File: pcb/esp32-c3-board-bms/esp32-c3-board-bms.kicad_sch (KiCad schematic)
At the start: 34 parts, among them P1 HW-613, P101 CAN, P102 BMS UART, P3 CONN_1, P4 CONN_1, P5 CONN_1, P6 CONN_1, U1 ESP32-C3-Waveshare, U102 TJA1050, U2 esp32-c3-ebay, U3 LP2985-3.3, U4 PC817, U5 DCDCConverter, U7 STIS0621

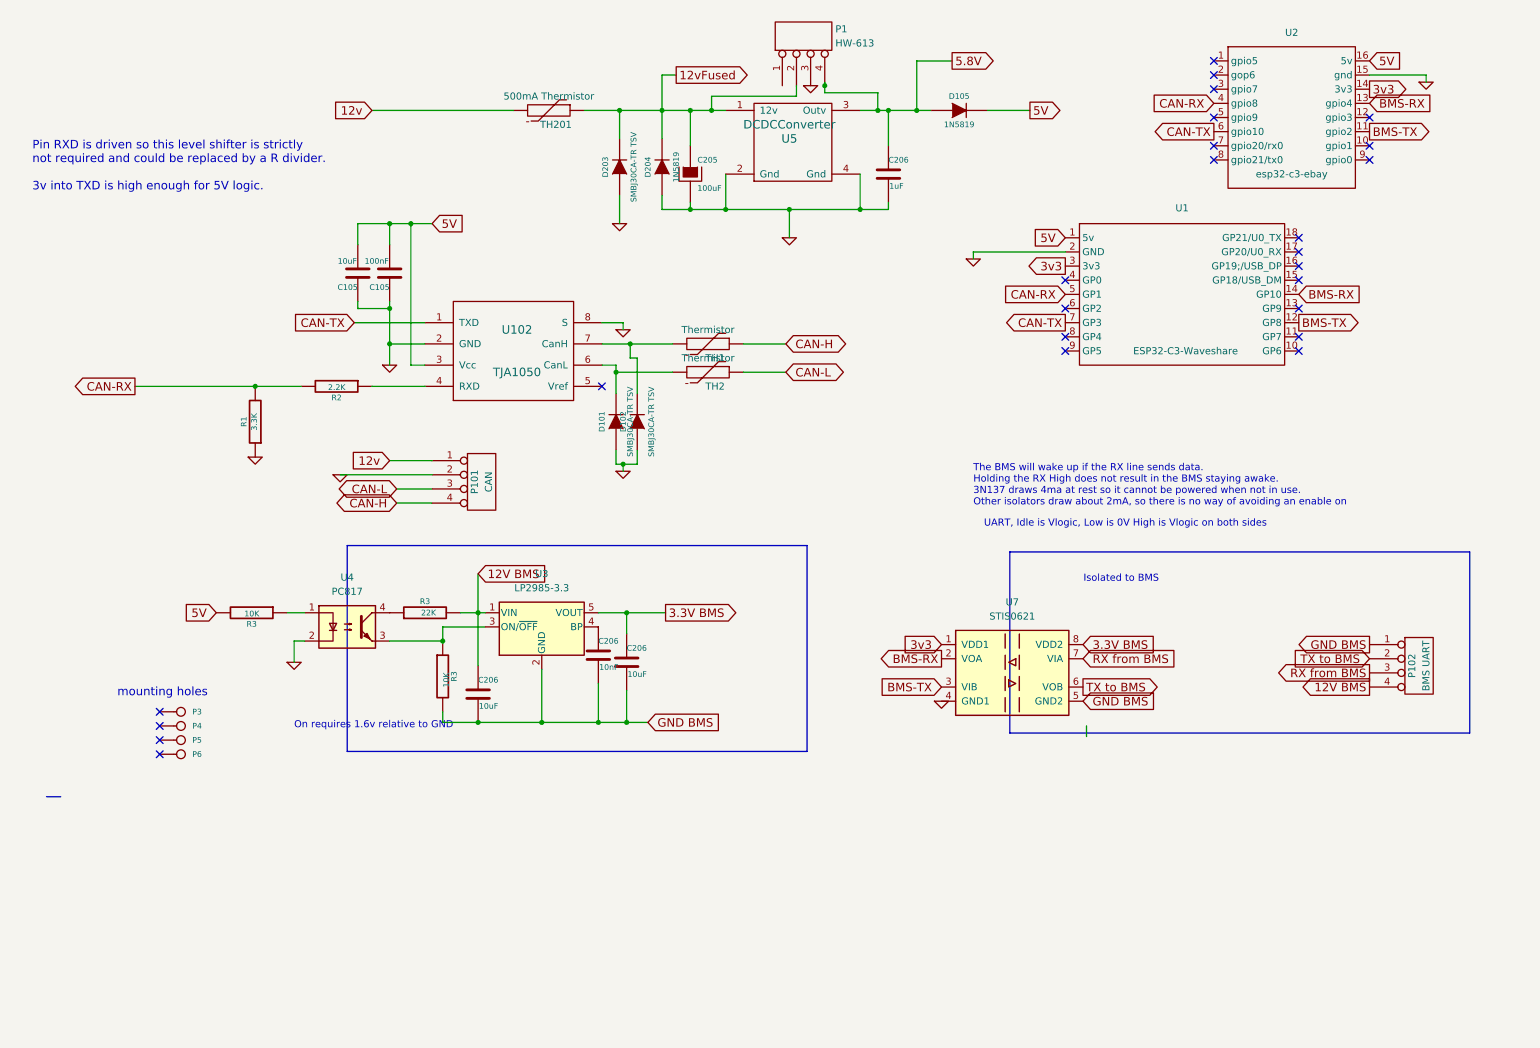
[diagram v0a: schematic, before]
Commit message: Board redesigned to be isolated from the can rather than bms
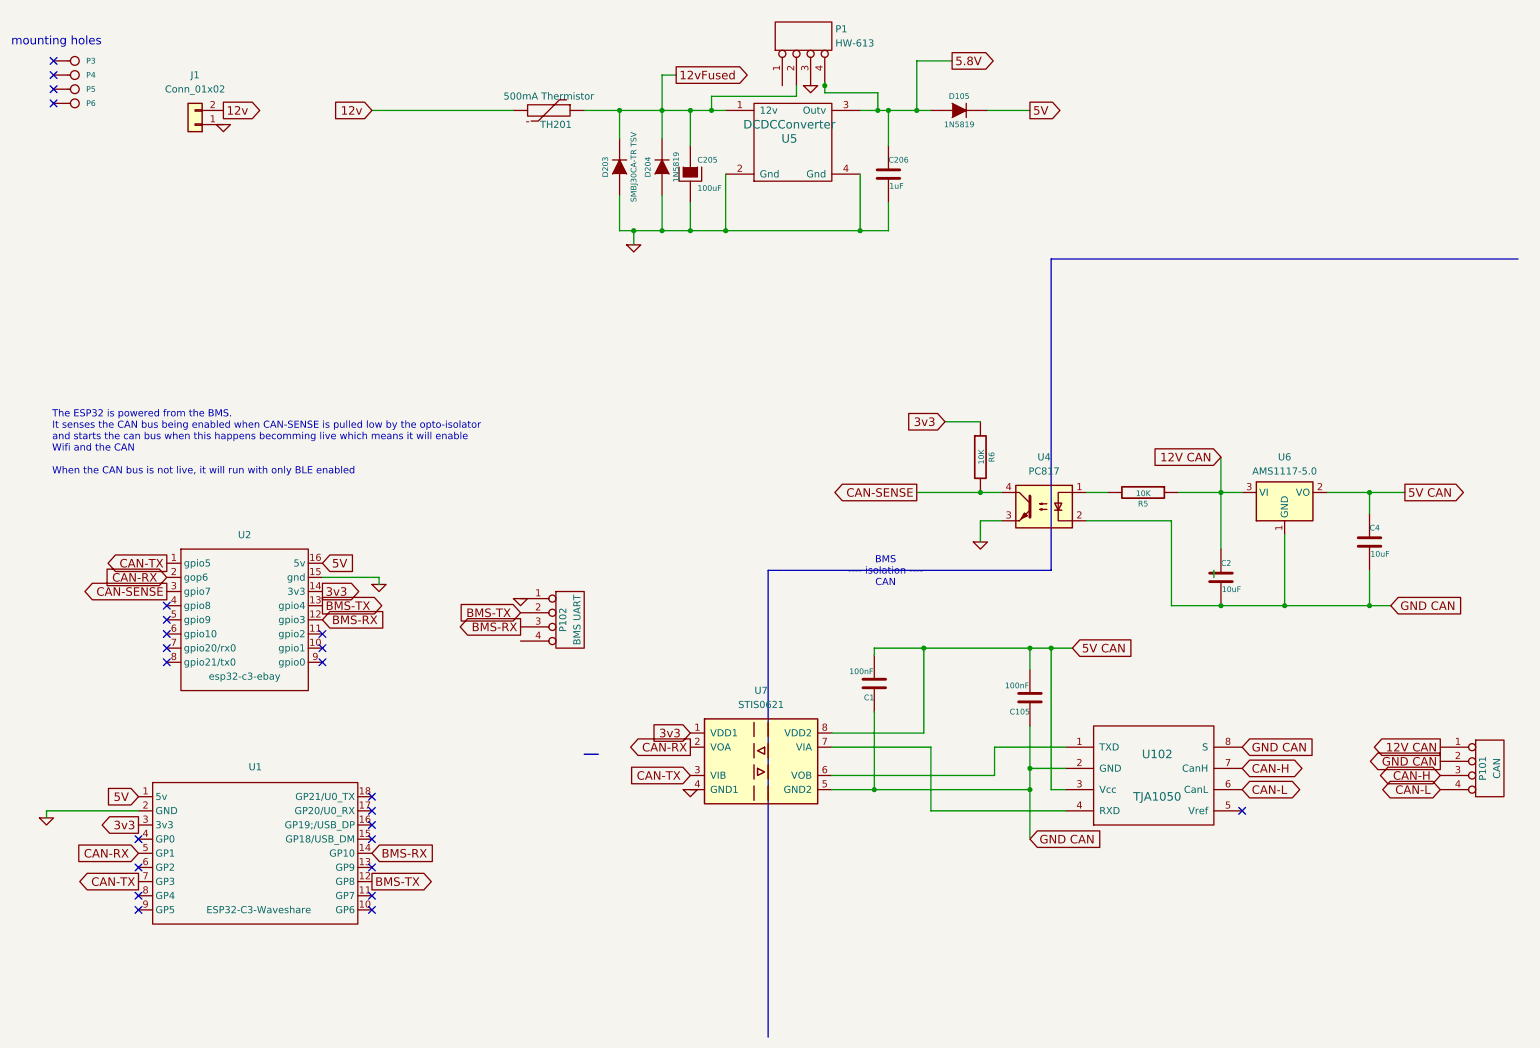
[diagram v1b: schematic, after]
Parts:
- removed C105, C206 (x2): 10uF, Capacitor_SMD:C_0805_2012Metric_Pad1.18x1.45mm_HandSolder, symbol device:C
- removed C206: 10nF, Capacitor_SMD:C_0805_2012Metric_Pad1.18x1.45mm_HandSolder, symbol device:C
- removed D101, D102: SMBJ30CA-TR TSV, Diode_SMD:D_SMB_Handsoldering, symbol device:DIODE
- removed R1: 3.3K, Resistor_SMD:R_0805_2012Metric_Pad1.20x1.40mm_HandSolder, symbol device:R
- removed R2: 2.2K, Resistor_SMD:R_0805_2012Metric_Pad1.20x1.40mm_HandSolder, symbol device:R
- removed R3: 22K, Resistor_SMD:R_0805_2012Metric_Pad1.20x1.40mm_HandSolder, symbol device:R
- removed R3 (x2): 10K, Resistor_SMD:R_0805_2012Metric_Pad1.20x1.40mm_HandSolder, symbol device:R
- removed TH1, TH2: Thermistor, Resistor_SMD:R_2010_5025Metric_Pad1.40x2.65mm_HandSolder, symbol device:THERMISTOR
- removed U3: LP2985-3.3, Package_TO_SOT_SMD:SOT-23-5, symbol Regulator_Linear:LP2985-3.3
- added C1: 100nF, Capacitor_SMD:C_0805_2012Metric_Pad1.18x1.45mm_HandSolder, symbol device:C
- added C2, C4: 10uF, Capacitor_SMD:C_0805_2012Metric_Pad1.18x1.45mm_HandSolder, symbol device:C
- added J1: Conn_01x02, Connector_JST:JST_XH_B2B-XH-A_1x02_P2.50mm_Vertical, symbol Connector_Generic:Conn_01x02
- added R5, R6: 10K, Resistor_SMD:R_0805_2012Metric_Pad1.20x1.40mm_HandSolder, symbol device:R
- added U6: AMS1117-5.0, Package_TO_SOT_SMD:SOT-223-3_TabPin2, symbol Regulator_Linear:AMS1117-5.0
- P102: footprint Connector_JST:JST_XH_S4B-XH-A_1x04_P2.50mm_Horizontal -> Connector_JST:JST_XH_B4B-XH-A_1x04_P2.50mm_Vertical
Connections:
- net 12v: now also J1.2 (Pin_2); no longer P101.1 (P1)
- net 3v3: now also R6.1
- net 5V: no longer C105.2, U102.3 (Vcc)
- net BMS-RX: now also P102.3 (P3), U2.12 (gpio3); no longer U2.13 (gpio4), U7.2 (VOA)
- net BMS-TX: now also P102.2 (P2), U2.13 (gpio4); no longer U2.11 (gpio2), U7.3 (VIB)
- net CAN-H: now also P101.3 (P3), U102.7 (CanH); no longer P101.4 (P4)
- net CAN-L: now also P101.4 (P4), U102.6 (CanL); no longer P101.3 (P3)
- net CAN-RX: now also U2.2 (gop6), U7.2 (VOA); no longer U2.4 (gpio8)
- net CAN-TX: now also U2.1 (gpio5), U7.3 (VIB); no longer U102.1 (TXD), U2.6 (gpio10)
- net GND: now also P102.1 (P1), U4.3, J1.1 (Pin_1); no longer C105.1, P101.2 (P2), U102.2 (GND), U102.8 (S), U4.2
- net at U102.4 (RXD): now also U7.7 (VIA)
- net CAN-SENSE: now reaches U4.4
- net CAN-SENSE: now also U2.3 (gpio7), R6.2
- net at U4.1: now also R5.2
- net 12V BMS: no longer names the net of P102.4 (P4)
- net 3.3V BMS renamed 5V CAN
- net 5V CAN: now also C105.2, U102.3 (Vcc), C1.2, C4.1, U6.2 (VO)
- net GND BMS renamed GND CAN
- net GND CAN: now also C105.1, P101.2 (P2), U102.2 (GND), U102.8 (S), U4.2, C1.1, C2.2, C4.2, U6.1 (GND); no longer P102.1 (P1)
- removed net RX from BMS: P102.3 (P3), U7.7 (VIA)
- net TX to BMS: no longer names the net of U7.6 (VOB)
- net TX to BMS: now also U102.1 (TXD); no longer P102.2 (P2)
- new net 12V CAN: C2.1, P101.1 (P1), R5.1, U6.3 (VI)
- no-connect marks 25 -> 24
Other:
- note added: "BMS ---- isolation ---- CAN"
- note added: "The ESP32 is powered from the BMS. It senses the CAN bus being enabled when CAN-SENSE is pulled low by the opto-isolator and starts the can bus when this happens becomming live which means it will enable Wifi and the CAN When the CAN bus is not live, it will run with only BLE enabled"
- note removed: "Isolated to BMS"
- note removed: "On requires 1.6v relative to GND"
- note removed: "Pin RXD is driven so this level shifter is strictly not required and could be replaced by a R divider. 3v into TXD is high enough for 5V logic."
- note removed: "The BMS will wake up if the RX line sends data. Holding the RX High does not result in the BMS staying awake. 3N137 draws 4ma at rest so it cannot be powered when not in use. Other isolators draw about 2mA, so there is no way of avoiding an enable on"
- note removed: "UART, Idle is Vlogic, Low is 0V High is Vlogic on both sides"
- moved on the sheet: C105, P101, P102, P3, P4, P5, P6, U1, U102, U2, U4, U7

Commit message: updated board, ready for fab
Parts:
- removed D105: 1N5819, Diode_SMD:D_1206_3216Metric_Pad1.42x1.75mm_HandSolder, symbol device:DIODE
- added J2: Conn_01x02, Connector_JST:JST_XH_B2B-XH-A_1x02_P2.50mm_Vertical, symbol Connector_Generic:Conn_01x02
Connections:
- net 5.8V is gone; now on net 5V: C206.1, P1.4 (P4), U5.3 (Outv)
- net 12v: now also J2.1 (Pin_1); no longer TH201.2
- new net 12v Switched: J2.2 (Pin_2), TH201.2
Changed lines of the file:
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@@
 	)
 	(junction
-		(at 176.53 29.21)
-		(diameter 0)
-		(color 0 0 0 0)
-	)
-	(junction
 		(at 231.14 118.11)
 		(diameter 0)
@@
 	(wire
 		(pts
-			(xy 189.23 29.21) (xy 196.85 29.21)
-		)
-		(stroke
-			(width 0)
-			(type default)
-		)
-	)
-	(wire
-		(pts
 			(xy 242.57 105.41) (xy 242.57 118.11)
 		)
@@
 	(wire
 		(pts
-			(xy 182.88 20.32) (xy 176.53 20.32)
-		)
-		(stroke
-			(width 0)
-			(type default)
-		)
-	)
-	(wire
-		(pts
 			(xy 207.01 102.87) (xy 222.25 102.87)
 		)
@@
 	(wire
 		(pts
-			(xy 176.53 20.32) (xy 176.53 29.21)
-		)
-		(stroke
-			(width 0)
-			(type default)
-		)
-	)
-	(wire
-		(pts
 			(xy 196.85 160.02) (xy 196.85 151.13)
 		)
@@
 	(wire
 		(pts
-			(xy 171.45 29.21) (xy 176.53 29.21)
+			(xy 171.45 29.21) (xy 196.85 29.21)
 		)
 		(stroke
@@
 	(wire
 		(pts
-			(xy 176.53 29.21) (xy 179.07 29.21)
-		)
-		(stroke
-			(width 0)
-			(type default)
-		)
-	)
-	(wire
-		(pts
 			(xy 257.81 97.79) (xy 264.16 97.79)
 		)
@@
 		)
 	)
+	(global_label "12v Switched"
+		(shape output)
+		(at 52.07 41.91 0)
+		(effects
+			(font
+				(size 1.524 1.524)
+			)
+			(justify left)
+		)
+		(property "Intersheetrefs" "${INTERSHEET_REFS}"
+			(at 52.07 41.91 0)
+			(effects
+				(font
+					(size 1.27 1.27)
+				)
+				(hide yes)
+			)
+		)
+	)
 	(global_label "BMS-RX"
 		(shape output)
@@
 		)
 	)
-	(global_label "5.8V"
-		(shape output)
-		(at 182.88 20.32 0)
-		(effects
-			(font
-				(size 1.524 1.524)
-			)
-			(justify left)
-		)
-		(property "Intersheetrefs" "${INTERSHEET_REFS}"
-			(at 182.88 20.32 0)
-			(effects
-				(font
-					(size 1.27 1.27)
-				)
-				(hide yes)
-			)
-		)
-	)
-	(global_label "12v"
+	(global_label "12v Switched"
 		(shape input)
 		(at 78.74 29.21 180)
@@
 		)
 	)
+	(global_label "12v"
+		(shape input)
+		(at 52.07 44.45 0)
+		(effects
+			(font
+				(size 1.524 1.524)
+			)
+			(justify left)
+		)
+		(property "Intersheetrefs" "${INTERSHEET_REFS}"
+			(at 52.07 44.45 0)
+			(effects
+				(font
+					(size 1.27 1.27)
+				)
+				(hide yes)
+			)
+		)
+	)
 	(global_label "CAN-RX"
 		(shape output)
@@
 	)
 	(symbol
-		(lib_id "device:DIODE")
-		(at 184.15 29.21 0)
-		(unit 1)
-		(exclude_from_sim no)
-		(in_bom yes)
-		(on_board yes)
-		(dnp no)
-		(property "Reference" "D105"
-			(at 184.15 26.67 0)
-			(effects
-				(font
-					(size 1.016 1.016)
-				)
-			)
-		)
-		(property "Value" "1N5819"
-			(at 184.15 31.75 0)
-			(effects
-				(font
-					(size 1.016 1.016)
-				)
-			)
-		)
-		(property "Footprint" "Diode_SMD:D_1206_3216Metric_Pad1.42x1.75mm_HandSolder"
-			(at 184.15 29.21 0)
-			(effects
-				(font
-					(size 1.524 1.524)
-				)
-				(hide yes)
-			)
-		)
-		(property "Datasheet" ""
-			(at 184.15 29.21 0)
-			(effects
-				(font
-					(size 1.524 1.524)
-				)
-			)
-		)
-		(property "Description" ""
-			(at 184.15 29.21 0)
-			(effects
-				(font
-					(size 1.27 1.27)
-				)
-			)
-		)
-		(pin "1"
-		)
-		(pin "2"
-		)
-		(instances
-			(project "ESP32CanBoard"
-				(path "/17502814-a097-4dea-91a7-aec909c8a89f"
-					(reference "D105")
-					(unit 1)
-				)
-			)
-			(project "esp32-c3-board"
-				(path "/f1c311d1-2fb5-46a9-8cac-10128a8ff086"
-					(reference "D105")
-					(unit 1)
-				)
-			)
-		)
-	)
-	(symbol
 		(lib_id "conn:CONN_4")
 		(at 279.4 147.32 0)
@@
 					(unit 1)
 				)
+			)
+		)
+	)
+	(symbol
+		(lib_id "Connector_Generic:Conn_01x02")
+		(at 46.99 44.45 180)
+		(unit 1)
+		(exclude_from_sim no)
+		(in_bom yes)
+		(on_board yes)
+		(dnp no)
+		(fields_autoplaced yes)
+		(property "Reference" "J2"
+			(at 46.99 35.56 0)
+			(effects
+				(font
+					(size 1.27 1.27)
+				)
+			)
+		)
+		(property "Value" "Conn_01x02"
+			(at 46.99 38.1 0)
+			(effects
+				(font
+					(size 1.27 1.27)
+				)
+			)
+		)
+		(property "Footprint" "Connector_JST:JST_XH_B2B-XH-A_1x02_P2.50mm_Vertical"
+			(at 46.99 44.45 0)
+			(effects
+				(font
+					(size 1.27 1.27)
+				)
+				(hide yes)
+			)
+		)
+		(property "Datasheet" "~"
+			(at 46.99 44.45 0)
+			(effects
+				(font
+					(size 1.27 1.27)
+				)
+				(hide yes)
+			)
+		)
+		(property "Description" "Generic connector, single row, 01x02, script generated (kicad-library-utils/schlib/autogen/connector/)"
+			(at 46.99 44.45 0)
+			(effects
+				(font
+					(size 1.27 1.27)
+				)
+				(hide yes)
+			)
+		)
+		(pin "1"
+		)
+		(pin "2"
+		)
+		(instances
+			(project "esp32-c3-board-bms"
+				(path "/f1c311d1-2fb5-46a9-8cac-10128a8ff086"
+					(reference "J2")
+					(unit 1)
+				)

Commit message: onboard MP2307 DCDC
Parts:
- added C10: 10nF, Capacitor_SMD:C_0805_2012Metric_Pad1.18x1.45mm_HandSolder, symbol Device:C
- added C11, C13: 100nF, Capacitor_SMD:C_0805_2012Metric_Pad1.18x1.45mm_HandSolder, symbol Device:C
- added C12, C14, C6: 10uF, Capacitor_SMD:C_0805_2012Metric_Pad1.18x1.45mm_HandSolder, symbol Device:C
- added C3: 10uF, Capacitor_SMD:C_0805_2012Metric_Pad1.18x1.45mm_HandSolder, symbol device:C
- added C5: 100nF, Capacitor_SMD:C_0805_2012Metric_Pad1.18x1.45mm_HandSolder, symbol device:C
- added C7: 180pF, Capacitor_SMD:C_0805_2012Metric_Pad1.18x1.45mm_HandSolder, symbol Device:C
- added C8: 6.8nF, Capacitor_SMD:C_0805_2012Metric_Pad1.18x1.45mm_HandSolder, symbol Device:C
- added C9: 18pF, Capacitor_SMD:C_0805_2012Metric_Pad1.18x1.45mm_HandSolder, symbol Device:C
- added L1: 22uH, Inductor_SMD:L_APV_ANR6045, symbol device:INDUCTOR
- added R1, R4: 47K, Resistor_SMD:R_0805_2012Metric_Pad1.20x1.40mm_HandSolder, symbol Device:R
- added R2: 10K, Resistor_SMD:R_0805_2012Metric_Pad1.20x1.40mm_HandSolder, symbol Device:R
- added R3: 8.45K, Resistor_SMD:R_0805_2012Metric_Pad1.20x1.40mm_HandSolder, symbol Device:R
- added R7: 100K, Resistor_SMD:R_0805_2012Metric_Pad1.20x1.40mm_HandSolder, symbol Device:R
- added R8: 1K, Resistor_SMD:R_0805_2012Metric_Pad1.20x1.40mm_HandSolder, symbol Device:R
- added U3: MP2307, Package_SO:SOIC-8-1EP_3.9x4.9mm_P1.27mm_EP2.62x3.51mm, symbol Regulator_Switching:MP2303ADN
- J1: value Conn_01x02 -> Power
- J2: value Conn_01x02 -> Switch
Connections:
- net 12vFused: now also C11.1, C12.1, R7.1, U3.2 (IN)
- net 3v3: now also C5.2
- net 5V: now also C14.1, C3.1, C6.1, C7.2, L1.2, R8.1
- net GND: now also C11.2, C12.2, C13.2, C14.2, C3.2, C5.1, C6.2, C8.1, C9.1, R2.1, R4.2, U3.4 (GND), U3.9 (Pad)
- new net: C7.1, R1.2, R2.2, U3.5 (FB)
- new net: C8.2, R3.1
- new net: R4.1, R7.2, U3.7 (EN)
- new net: C10.1, U3.1 (BS)
- new net: C10.2, L1.1, U3.3 (SW)
- new net: C9.2, R3.2, U3.6 (COMP)
- new net: C13.1, U3.8 (SS)
- new net: R1.1, R8.2
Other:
- note added: "VOut = 0.925 * (R1+R8+R2)/R2 0.912*(26.1+5.23)/5.23=5.46V 0.912*(47+10)/10=5.19V <<<< no diode 0.912*(47+1+10)/10=5.28V 0.912*(47+2.2+10)/10=5.39 0.912*(47+3.3+10)/10=5.49 0.912*(47+4.7+10)/10=5.62 0.912*(47+10+10)/10=5.62"
- moved on the sheet: C205, C206, D203, D204, J1, J2, P1, TH201, U5
